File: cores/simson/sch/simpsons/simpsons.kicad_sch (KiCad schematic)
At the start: 12 parts, among them CN1 Conn_02x32_Row_Letter_First, J2 Conn_01x15_Pin, J4 Conn_01x15_Pin, U3 JAMMA HARNESS

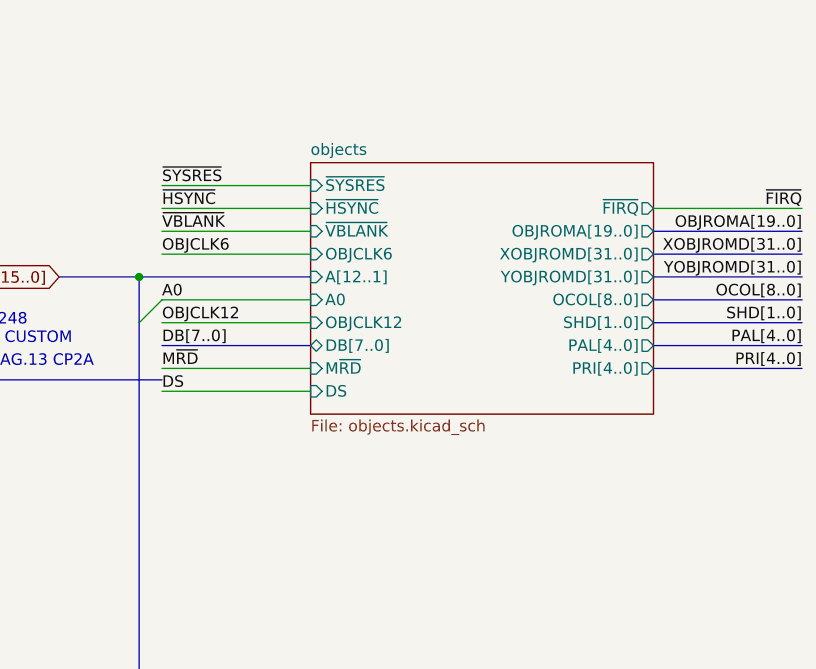
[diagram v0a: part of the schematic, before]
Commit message: riders: xmen address decoder xmen sch: fixed connections/cosmetic changes
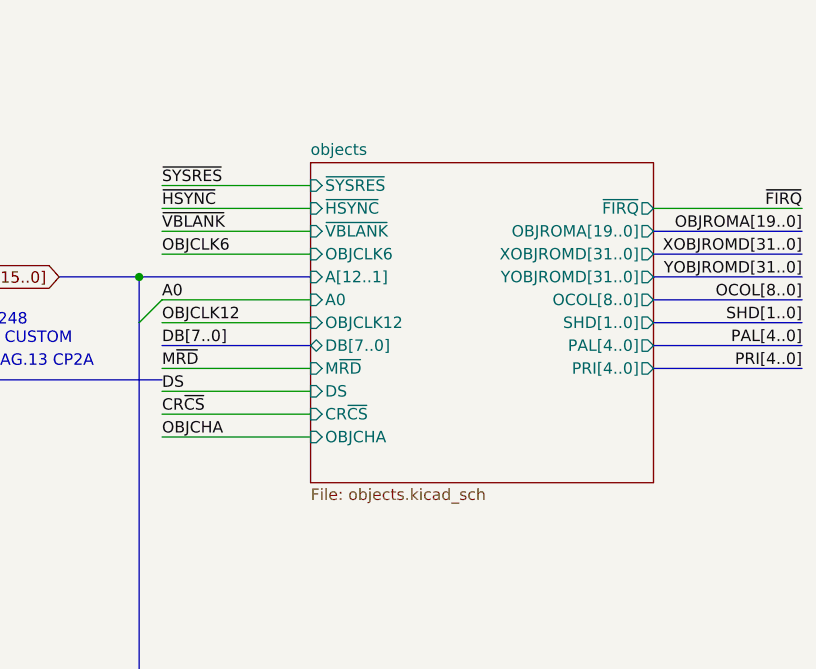
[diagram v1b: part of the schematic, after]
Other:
- sheet objects ports: added CR~{CS}, OBJCHA; removed none
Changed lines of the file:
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@@
 		)
 	)
+	(wire
+		(pts
+			(xy 236.22 82.55) (xy 252.73 82.55)
+		)
+		(stroke
+			(width 0)
+			(type default)
+		)
+	)
 	(bus
 		(pts
@@
 	(wire
 		(pts
+			(xy 236.22 85.09) (xy 252.73 85.09)
+		)
+		(stroke
+			(width 0)
+			(type default)
+		)
+	)
+	(wire
+		(pts
 			(xy 140.97 176.53) (xy 140.97 189.23)
 		)
@@
 		)
 	)
+	(label "OBJCHA"
+		(at 236.22 85.09 0)
+		(fields_autoplaced yes)
+		(effects
+			(font
+				(size 1.27 1.27)
+			)
+			(justify left bottom)
+		)
+	)
 	(label "XOBJROMD25"
 		(at 149.86 226.06 90)
@@
 		)
 	)
+	(label "CR~{CS}"
+		(at 236.22 82.55 0)
+		(fields_autoplaced yes)
+		(effects
+			(font
+				(size 1.27 1.27)
+			)
+			(justify left bottom)
+		)
+	)
 	(label "XOBJROMD13"
 		(at 149.86 271.78 90)
@@
 	(sheet
 		(at 252.73 54.61)
-		(size 38.1 27.94)
+		(size 38.1 35.56)
 		(fields_autoplaced yes)
 		(stroke
@@
 		)
 		(property "Sheetfile" "objects.kicad_sch"
-			(at 252.73 83.1346 0)
+			(at 252.73 90.7546 0)
 			(effects
 				(font
@@
 			(effects
 				(font
+					(size 1.27 1.27)
+				)
+				(justify left)
+			)
+		)
+		(pin "CR~{CS}" input
+			(at 252.73 82.55 180)
+			(effects
+				(font
+					(size 1.27 1.27)
+				)
+				(justify left)
+			)
+		)
+		(pin "OBJCHA" input
+			(at 252.73 85.09 180)
+			(effects
+				(font

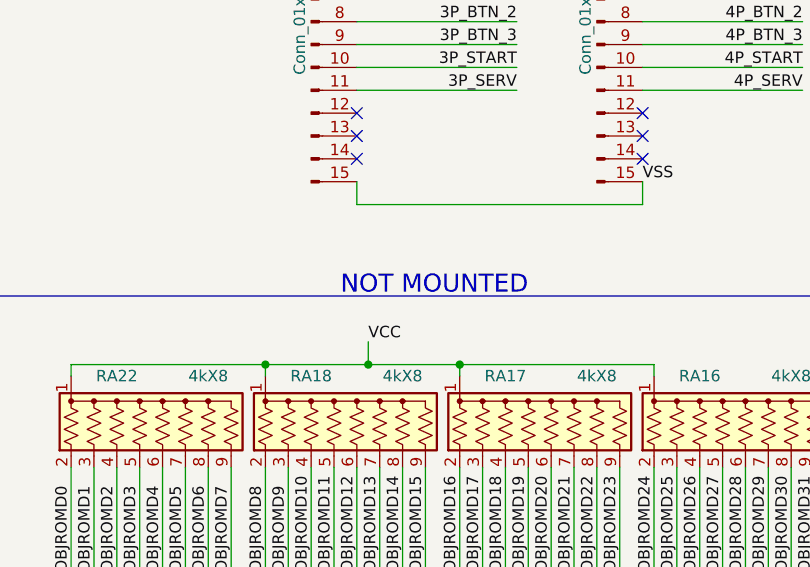
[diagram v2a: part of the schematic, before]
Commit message: sch: not mounted -> not populated
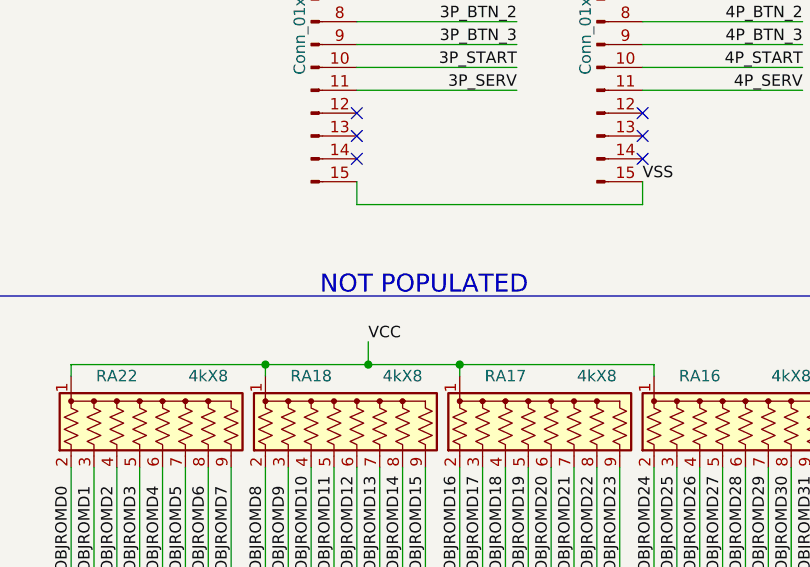
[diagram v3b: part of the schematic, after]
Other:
- note added: "NOT POPULATED"
- note removed: "NOT MOUNTED"
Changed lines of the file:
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@@
 		)
 	)
-	(text "NOT MOUNTED"
+	(text "NOT POPULATED"
 		(exclude_from_sim no)
 		(at 133.35 157.48 0)
